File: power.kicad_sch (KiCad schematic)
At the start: 42 parts, among them J201 USBC, Q201 2N7002, Q202 BSS84, SW201 PWR_ON, U201 MAX17043G+T, U202 MCP73831-3-OT, U203 LM3670MF

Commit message: Footprint selection
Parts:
- C201, C202, C203, C204, C205, C206, C207, C208, C209: footprint Capacitor_SMD:C_0805_2012Metric_Pad1.18x1.45mm_HandSolder -> Capacitor_SMD:C_1206_3216Metric_Pad1.33x1.80mm_HandSolder
- C210: footprint Capacitor_SMD:C_0805_2012Metric_Pad1.18x1.45mm_HandSolder -> Capacitor_Tantalum_SMD:CP_EIA-6032-20_AVX-F_Pad2.25x2.35mm_HandSolder
- D201, D202: footprint Diode_SMD:D_0805_2012Metric_Pad1.15x1.40mm_HandSolder -> Diode_SMD:D_1206_3216Metric_Pad1.42x1.75mm_HandSolder
- D203, D204: footprint LED_SMD:LED_0805_2012Metric_Pad1.15x1.40mm_HandSolder -> LED_SMD:LED_1206_3216Metric_Pad1.42x1.75mm_HandSolder
- Q201, Q202: footprint Package_TO_SOT_SMD:SOT-23 -> Package_TO_SOT_SMD:SOT-23W_Handsoldering
- R201, R202, R203, R204, R205, R206, R207, R208, R209, R210, R211, R212, R213, R214: footprint Resistor_SMD:R_0805_2012Metric_Pad1.20x1.40mm_HandSolder -> Resistor_SMD:R_1206_3216Metric_Pad1.30x1.75mm_HandSolder
- TP1, TP2, TP3, TP4, TP5: footprint (none) -> TestPoint:TestPoint_Pad_D1.0mm
- U201: footprint MAX17043:21-0174B_MXM -> lib:21-0174B_MXM
- U202: footprint Package_TO_SOT_SMD:SOT-23-5 -> Package_TO_SOT_SMD:SOT-23-5_HandSoldering
- U203: footprint Package_TO_SOT_SMD:TSOT-23-5 -> Package_TO_SOT_SMD:TSOT-23-5_HandSoldering
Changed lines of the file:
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@@
 			)
 		)
-		(property "Footprint" "Resistor_SMD:R_0805_2012Metric_Pad1.20x1.40mm_HandSolder"
+		(property "Footprint" "Resistor_SMD:R_1206_3216Metric_Pad1.30x1.75mm_HandSolder"
 			(at 172.212 146.05 90)
 			(effects
@@
 			)
 		)
-		(property "Footprint" "Capacitor_SMD:C_0805_2012Metric_Pad1.18x1.45mm_HandSolder"
+		(property "Footprint" "Capacitor_SMD:C_1206_3216Metric_Pad1.33x1.80mm_HandSolder"
 			(at 140.6652 67.31 0)
 			(effects
@@
 			)
 		)
-		(property "Footprint" "Resistor_SMD:R_0805_2012Metric_Pad1.20x1.40mm_HandSolder"
+		(property "Footprint" "Resistor_SMD:R_1206_3216Metric_Pad1.30x1.75mm_HandSolder"
 			(at 80.518 80.01 90)
 			(effects
@@
 			)
 		)
-		(property "Footprint" ""
+		(property "Footprint" "TestPoint:TestPoint_Pad_D1.0mm"
 			(at 189.23 73.66 0)
 			(effects
@@
 			)
 		)
-		(property "Footprint" "Capacitor_SMD:C_0805_2012Metric_Pad1.18x1.45mm_HandSolder"
+		(property "Footprint" "Capacitor_SMD:C_1206_3216Metric_Pad1.33x1.80mm_HandSolder"
 			(at 213.0552 82.55 0)
 			(effects
@@
 			)
 		)
-		(property "Footprint" "MAX17043:21-0174B_MXM"
+		(property "Footprint" "lib:21-0174B_MXM"
 			(at 90.17 140.97 0)
 			(effects
@@
 			)
 		)
-		(property "Footprint" "Resistor_SMD:R_0805_2012Metric_Pad1.20x1.40mm_HandSolder"
+		(property "Footprint" "Resistor_SMD:R_1206_3216Metric_Pad1.30x1.75mm_HandSolder"
 			(at 102.362 80.01 90)
 			(effects
@@
 			)
 		)
-		(property "Footprint" "Resistor_SMD:R_0805_2012Metric_Pad1.20x1.40mm_HandSolder"
+		(property "Footprint" "Resistor_SMD:R_1206_3216Metric_Pad1.30x1.75mm_HandSolder"
 			(at 209.042 147.32 90)
 			(effects
@@
 			)
 		)
-		(property "Footprint" "Resistor_SMD:R_0805_2012Metric_Pad1.20x1.40mm_HandSolder"
+		(property "Footprint" "Resistor_SMD:R_1206_3216Metric_Pad1.30x1.75mm_HandSolder"
 			(at 103.378 80.01 90)
 			(effects
@@
 			)
 		)
-		(property "Footprint" ""
+		(property "Footprint" "TestPoint:TestPoint_Pad_D1.0mm"
 			(at 147.32 57.15 0)
 			(effects
@@
 			)
 		)
-		(property "Footprint" "Resistor_SMD:R_0805_2012Metric_Pad1.20x1.40mm_HandSolder"
+		(property "Footprint" "Resistor_SMD:R_1206_3216Metric_Pad1.30x1.75mm_HandSolder"
 			(at 74.93 128.778 90)
 			(effects
@@
 			)
 		)
-		(property "Footprint" "Package_TO_SOT_SMD:SOT-23"
+		(property "Footprint" "Package_TO_SOT_SMD:SOT-23W_Handsoldering"
 			(at 196.85 133.985 0)
 			(effects
@@
 			)
 		)
-		(property "Footprint" "LED_SMD:LED_0805_2012Metric_Pad1.15x1.40mm_HandSolder"
+		(property "Footprint" "LED_SMD:LED_1206_3216Metric_Pad1.42x1.75mm_HandSolder"
 			(at 252.73 128.27 0)
 			(effects
@@
 			)
 		)
-		(property "Footprint" ""
+		(property "Footprint" "TestPoint:TestPoint_Pad_D1.0mm"
 			(at 255.27 124.46 0)
 			(effects
@@
 			)
 		)
-		(property "Footprint" "Capacitor_SMD:C_0805_2012Metric_Pad1.18x1.45mm_HandSolder"
+		(property "Footprint" "Capacitor_SMD:C_1206_3216Metric_Pad1.33x1.80mm_HandSolder"
 			(at 83.5152 134.62 0)
 			(effects
@@
 			)
 		)
-		(property "Footprint" "Resistor_SMD:R_0805_2012Metric_Pad1.20x1.40mm_HandSolder"
+		(property "Footprint" "Resistor_SMD:R_1206_3216Metric_Pad1.30x1.75mm_HandSolder"
 			(at 181.102 130.81 90)
 			(effects
@@
 			)
 		)
-		(property "Footprint" "Capacitor_SMD:C_0805_2012Metric_Pad1.18x1.45mm_HandSolder"
+		(property "Footprint" "Capacitor_SMD:C_1206_3216Metric_Pad1.33x1.80mm_HandSolder"
 			(at 72.0852 170.18 0)
 			(effects
@@
 			)
 		)
-		(property "Footprint" "Resistor_SMD:R_0805_2012Metric_Pad1.20x1.40mm_HandSolder"
+		(property "Footprint" "Resistor_SMD:R_1206_3216Metric_Pad1.30x1.75mm_HandSolder"
 			(at 250.952 137.16 90)
 			(effects
@@
 			)
 		)
-		(property "Footprint" "Capacitor_SMD:C_0805_2012Metric_Pad1.18x1.45mm_HandSolder"
+		(property "Footprint" "Capacitor_SMD:C_1206_3216Metric_Pad1.33x1.80mm_HandSolder"
 			(at 135.5852 67.31 0)
 			(effects
@@
 			)
 		)
-		(property "Footprint" "Resistor_SMD:R_0805_2012Metric_Pad1.20x1.40mm_HandSolder"
+		(property "Footprint" "Resistor_SMD:R_1206_3216Metric_Pad1.30x1.75mm_HandSolder"
 			(at 130.302 135.89 90)
 			(effects
@@
 			)
 		)
-		(property "Footprint" "Package_TO_SOT_SMD:SOT-23"
+		(property "Footprint" "Package_TO_SOT_SMD:SOT-23W_Handsoldering"
 			(at 185.42 144.145 0)
 			(effects
@@
 			)
 		)
-		(property "Footprint" "Capacitor_SMD:C_0805_2012Metric_Pad1.18x1.45mm_HandSolder"
+		(property "Footprint" "Capacitor_Tantalum_SMD:CP_EIA-6032-20_AVX-F_Pad2.25x2.35mm_HandSolder"
 			(at 242.2652 135.89 0)
 			(effects
@@
 			)
 		)
-		(property "Footprint" "LED_SMD:LED_0805_2012Metric_Pad1.15x1.40mm_HandSolder"
+		(property "Footprint" "LED_SMD:LED_1206_3216Metric_Pad1.42x1.75mm_HandSolder"
 			(at 199.39 69.85 0)
 			(effects
@@
 			)
 		)
-		(property "Footprint" "Resistor_SMD:R_0805_2012Metric_Pad1.20x1.40mm_HandSolder"
+		(property "Footprint" "Resistor_SMD:R_1206_3216Metric_Pad1.30x1.75mm_HandSolder"
 			(at 101.092 71.12 90)
 			(effects
@@
 			)
 		)
-		(property "Footprint" "Capacitor_SMD:C_0805_2012Metric_Pad1.18x1.45mm_HandSolder"
+		(property "Footprint" "Capacitor_SMD:C_1206_3216Metric_Pad1.33x1.80mm_HandSolder"
 			(at 202.8952 116.84 0)
 			(effects
@@
 			)
 		)
-		(property "Footprint" ""
+		(property "Footprint" "TestPoint:TestPoint_Pad_D1.0mm"
 			(at 196.85 66.04 0)
 			(effects
@@
 			)
 		)
-		(property "Footprint" "Diode_SMD:D_0805_2012Metric_Pad1.15x1.40mm_HandSolder"
+		(property "Footprint" "Diode_SMD:D_1206_3216Metric_Pad1.42x1.75mm_HandSolder"
 			(at 173.99 69.85 0)
 			(effects
@@
 			)
 		)
-		(property "Footprint" "Capacitor_SMD:C_0805_2012Metric_Pad1.18x1.45mm_HandSolder"
+		(property "Footprint" "Capacitor_SMD:C_1206_3216Metric_Pad1.33x1.80mm_HandSolder"
 			(at 168.6052 81.28 0)
 			(effects
@@
 			)
 		)
-		(property "Footprint" "Resistor_SMD:R_0805_2012Metric_Pad1.20x1.40mm_HandSolder"
+		(property "Footprint" "Resistor_SMD:R_1206_3216Metric_Pad1.30x1.75mm_HandSolder"
 			(at 137.922 83.82 90)
 			(effects
@@
 			)
 		)
-		(property "Footprint" "Package_TO_SOT_SMD:TSOT-23-5"
+		(property "Footprint" "Package_TO_SOT_SMD:TSOT-23-5_HandSoldering"
 			(at 219.71 133.35 0)
 			(effects
@@
 			)
 		)
-		(property "Footprint" "Resistor_SMD:R_0805_2012Metric_Pad1.20x1.40mm_HandSolder"
+		(property "Footprint" "Resistor_SMD:R_1206_3216Metric_Pad1.30x1.75mm_HandSolder"
 			(at 78.232 71.12 90)
 			(effects
@@
 			)
 		)
-		(property "Footprint" "Resistor_SMD:R_0805_2012Metric_Pad1.20x1.40mm_HandSolder"
+		(property "Footprint" "Resistor_SMD:R_1206_3216Metric_Pad1.30x1.75mm_HandSolder"
 			(at 197.612 81.28 90)
 			(effects
@@
 			)
 		)
-		(property "Footprint" "Capacitor_SMD:C_0805_2012Metric_Pad1.18x1.45mm_HandSolder"
+		(property "Footprint" "Capacitor_SMD:C_1206_3216Metric_Pad1.33x1.80mm_HandSolder"
 			(at 65.7352 170.18 0)
 			(effects
@@
 			)
 		)
-		(property "Footprint" ""
+		(property "Footprint" "TestPoint:TestPoint_Pad_D1.0mm"
 			(at 204.47 142.24 0)
 			(effects
@@
 			)
 		)
-		(property "Footprint" "Capacitor_SMD:C_0805_2012Metric_Pad1.18x1.45mm_HandSolder"
+		(property "Footprint" "Capacitor_SMD:C_1206_3216Metric_Pad1.33x1.80mm_HandSolder"
 			(at 196.5452 116.84 0)
 			(effects
@@
 			)
 		)
-		(property "Footprint" "Diode_SMD:D_0805_2012Metric_Pad1.15x1.40mm_HandSolder"
+		(property "Footprint" "Diode_SMD:D_1206_3216Metric_Pad1.42x1.75mm_HandSolder"
 			(at 163.83 66.04 0)
 			(effects
@@
 			)
 		)
-		(property "Footprint" "Package_TO_SOT_SMD:SOT-23-5"
+		(property "Footprint" "Package_TO_SOT_SMD:SOT-23-5_HandSoldering"
 			(at 153.67 82.55 0)
 			(effects
@@
 			)
 		)
-		(property "Footprint" "Resistor_SMD:R_0805_2012Metric_Pad1.20x1.40mm_HandSolder"
+		(property "Footprint" "Resistor_SMD:R_1206_3216Metric_Pad1.30x1.75mm_HandSolder"
 			(at 79.502 80.01 90)
 			(effects

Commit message: Polarized Tantalum capacitor symbol
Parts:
- removed C210: 10u, Capacitor_Tantalum_SMD:CP_EIA-6032-20_AVX-F_Pad2.25x2.35mm_HandSolder, symbol Device:C
- added C210: 10u, Capacitor_Tantalum_SMD:CP_EIA-6032-28_Kemet-C_HandSolder, symbol Device:C_Polarized
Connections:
- net GND: now also C210.2
- net VCC: now also C210.1
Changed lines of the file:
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@@
+	)
+	(symbol
+		(lib_id "Device:C_Polarized")
+		(at 241.3 132.08 0)
+		(unit 1)
+		(exclude_from_sim no)
+		(in_bom yes)
+		(on_board yes)
+		(dnp no)
+		(fields_autoplaced yes)
+		(property "Reference" "C210"
+			(at 245.11 129.9209 0)
+			(effects
+				(font
+					(size 1.27 1.27)
+				)
+				(justify left)
+			)
+		)
+		(property "Value" "10u"
+			(at 245.11 132.4609 0)
+			(effects
+				(font
+					(size 1.27 1.27)
+				)
+				(justify left)
+			)
+		)
+		(property "Footprint" "Capacitor_Tantalum_SMD:CP_EIA-6032-28_Kemet-C_HandSolder"
+			(at 242.2652 135.89 0)
+			(effects
+				(font
+					(size 1.27 1.27)
+				)
+				(hide yes)
+			)
+		)
+		(property "Datasheet" "~"
+			(at 241.3 132.08 0)
+			(effects
+				(font
+					(size 1.27 1.27)
+				)
+				(hide yes)
+			)
+		)
+		(property "Description" "Polarized capacitor"
+			(at 241.3 132.08 0)
+			(effects
+				(font
+					(size 1.27 1.27)
+				)
+				(hide yes)
+			)
+		)
+		(pin "2"
+		)
+		(pin "1"
+		)
+		(instances
+			(project ""
+				(path "/16b3e55a-9d75-49bf-a6fe-25414eb3d7da/8f87360a-db94-4899-a1b3-392efb8a6c91"
+					(reference "C210")
+					(unit 1)
+				)
+			)
+		)
 	)
 	(symbol
@@
 					(unit 1)
 				)
-			)
-		)
-	)
-	(symbol
-		(lib_id "Device:C")
-		(at 241.3 132.08 0)
-		(unit 1)
-		(exclude_from_sim no)
-		(in_bom yes)
-		(on_board yes)
-		(dnp no)
-		(fields_autoplaced yes)
-		(property "Reference" "C210"
-			(at 245.11 130.8099 0)
-			(effects
-				(font
-					(size 1.27 1.27)
-				)
-				(justify left)
-			)
-		)
-		(property "Value" "10u"
-			(at 245.11 133.3499 0)
-			(effects
-				(font
-					(size 1.27 1.27)
-				)
-				(justify left)
-			)
-		)
-		(property "Footprint" "Capacitor_Tantalum_SMD:CP_EIA-6032-20_AVX-F_Pad2.25x2.35mm_HandSolder"
-			(at 242.2652 135.89 0)
-			(effects
-				(font
-					(size 1.27 1.27)
-				)
-				(hide yes)
-			)
-		)
-		(property "Datasheet" "~"
-			(at 241.3 132.08 0)
-			(effects
-				(font
-					(size 1.27 1.27)
-				)
-				(hide yes)
-			)
-		)
-		(property "Description" "Unpolarized capacitor"
-			(at 241.3 132.08 0)
-			(effects
-				(font
-					(size 1.27 1.27)
-				)
-				(hide yes)
-			)
-		)
-		(pin "1"
-		)
-		(pin "2"
-		)
-		(instances
-			(project ""
-				(path "/16b3e55a-9d75-49bf-a6fe-25414eb3d7da/8f87360a-db94-4899-a1b3-392efb8a6c91"
-					(reference "C210")
-					(unit 1)
-				)

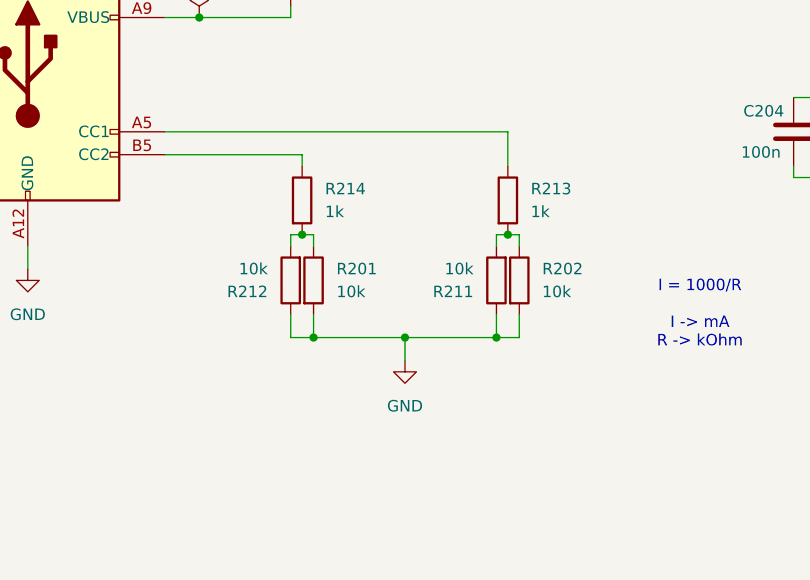
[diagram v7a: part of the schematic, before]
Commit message: USB 10k//10k CC resistors
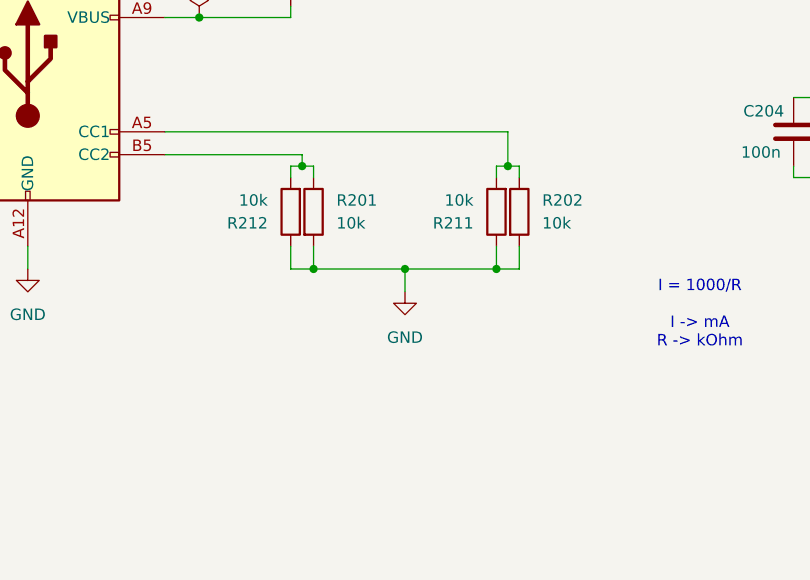
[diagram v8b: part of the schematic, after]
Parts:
- removed R213, R214: 1k, Resistor_SMD:R_1206_3216Metric_Pad1.30x1.75mm_HandSolder, symbol Device:R
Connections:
- net at R201.1, R212.2: now also J201.B5 (CC2)
- net at R202.1, R211.2: now also J201.A5 (CC1)
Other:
- moved on the sheet: R201, R202, R211, R212
